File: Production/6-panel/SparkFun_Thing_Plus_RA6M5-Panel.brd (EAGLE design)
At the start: 83.3 x 181.6 mm, 1092 parts, among them J1 USB Female Type C Connector, J11 QWIIC_RA, J12 MICRO-SDFRICTION, J13 CONN_03X2, J15 THING_PLUS_LOGICAL, J16 USB Female Type C Connector, J18 QWIIC_RA, J19 MICRO-SDFRICTION, J2 THING_PLUS_LOGICAL, J20 CONN_03X2, J22 THING_PLUS_LOGICAL, J23 USB Female Type C Connector, J25 QWIIC_RA, J26 MICRO-SDFRICTION, J27 CONN_03X2, J29 THING_PLUS_LOGICAL, J3 QWIIC_RA, J30 USB Female Type C Connector, J32 QWIIC_RA, J33 MICRO-SDFRICTION, J34 CONN_03X2, J36 THING_PLUS_LOGICAL, J37 USB Female Type C Connector, J39 QWIIC_RA, J4 CONN_03X2, J40 MICRO-SDFRICTION, J41 CONN_03X2, J7 MICRO-SDFRICTION, J8 THING_PLUS_LOGICAL, J9 USB Female Type C Connector, Q1 20V/4.2A/52mΩ/1.4W, Q10 20V/4.2A/52mΩ/1.4W, Q11 20V/4.2A/52mΩ/1.4W, Q12 20V/4.2A/52mΩ/1.4W, Q2 20V/4.2A/52mΩ/1.4W, Q3 20V/4.2A/52mΩ/1.4W, Q4 20V/4.2A/52mΩ/1.4W, Q5 20V/4.2A/52mΩ/1.4W, Q6 20V/4.2A/52mΩ/1.4W, Q7 20V/4.2A/52mΩ/1.4W, Q8 20V/4.2A/52mΩ/1.4W, Q9 20V/4.2A/52mΩ/1.4W, U1 R7FA6M5, U10 MCP73831, U11 MAX17048, U12 DA14531MOD, U13 MX25L12833F 128Mb, U14 R7FA6M5, U15 RT9080-33GJ5, U16 LM66200, U17 RT9080-33GJ5, U18 MCP73831, U19 MAX17048, U2 DA14531MOD, U20 DA14531MOD, U21 MX25L12833F 128Mb, U22 R7FA6M5, U23 RT9080-33GJ5, U24 LM66200, U25 RT9080-33GJ5, U26 MCP73831, U27 MAX17048, U28 DA14531MOD, U29 MX25L12833F 128Mb, U3 MCP73831, U30 R7FA6M5, U31 RT9080-33GJ5, U32 LM66200, U33 RT9080-33GJ5, U34 MCP73831, U35 MAX17048, U36 DA14531MOD, U37 MX25L12833F 128Mb, U38 R7FA6M5, U39 RT9080-33GJ5, U4 RT9080-33GJ5, U40 LM66200, U41 RT9080-33GJ5, U42 MCP73831, U43 MAX17048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

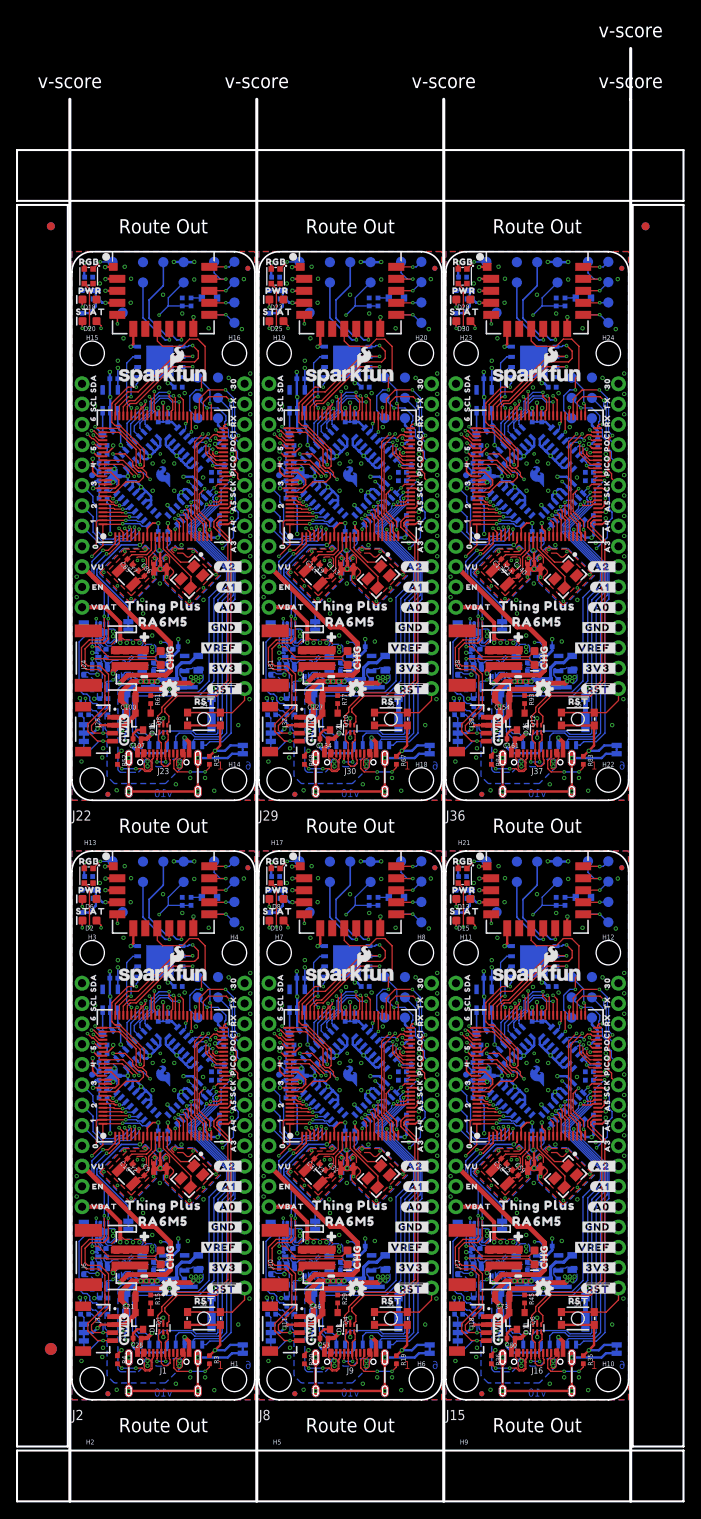
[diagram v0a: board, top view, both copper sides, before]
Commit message: Repanelize post reds review.
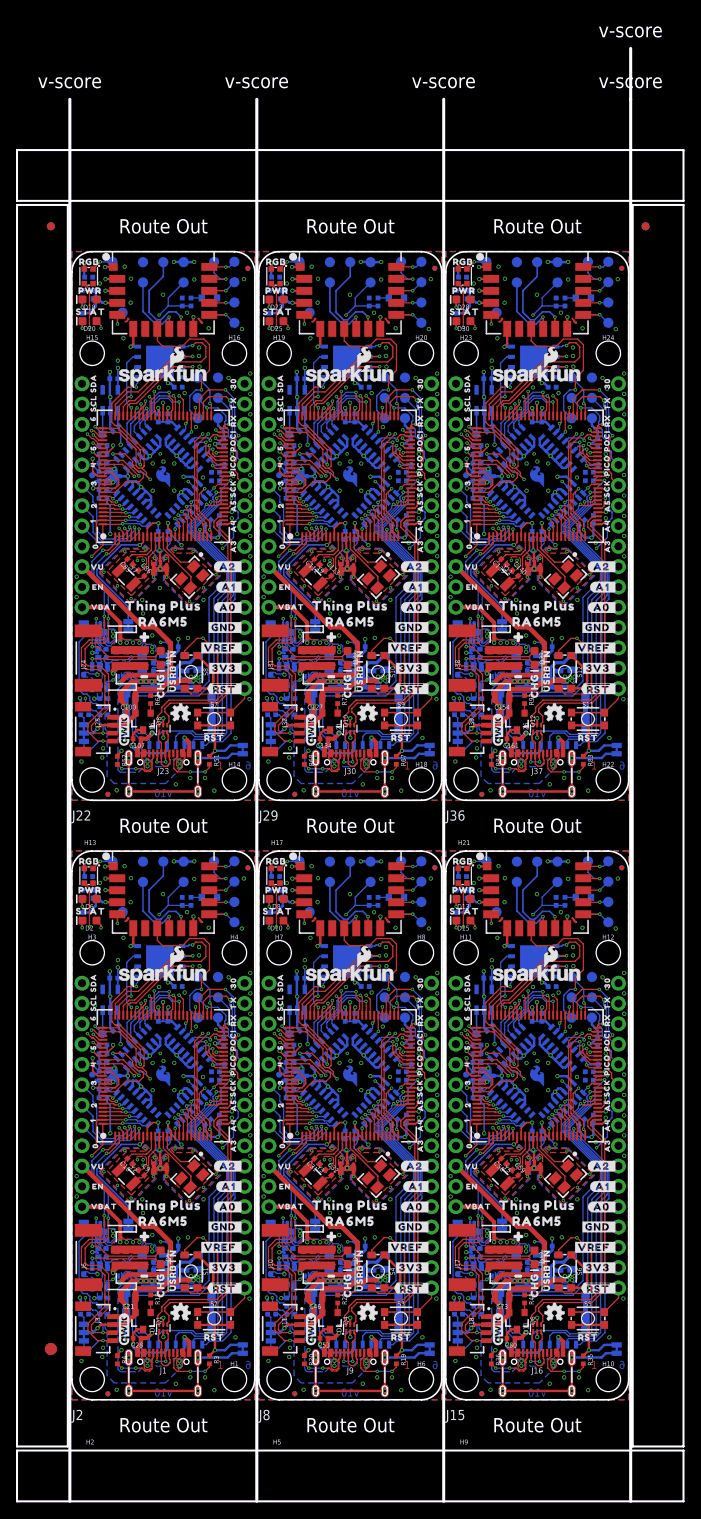
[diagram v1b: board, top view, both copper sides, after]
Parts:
- added S10, S12, S8: USER, SparkFun-Switches:TACTILE_SWITCH_SMD_4.6X2.8MM
- added S11, S7, S9: RESET, SparkFun-Switches:TACTILE_SWITCH_SMD_4.6X2.8MM
- added U$457: (no value), output:30
- added U$458: (no value), output:20
- added U$459: (no value), output:#1#0
- added U$460: (no value), output:#0#0
- added U$461: (no value), output:#USRBTN#0
- added U$462: (no value), output:#_VR#0
- S1, S4, S6: value RESET -> USER
- U$100, U$199: device output:SDA0 -> output:TX0
- U$101, U$200: device output:SCL0 -> output:SDA0
- U$102: device output:VU0 -> output:SCL0
- U$103: device output:EN0 -> output:VU0
- U$104: device output:VBAT0 -> output:EN0
- U$105: device output:#PWR#0 -> output:VBAT0
- U$106: device output:#BAT#0 -> output:#PWR#0
- U$107: device output:#SHLD#0 -> output:#BAT#0
- U$108: device output:#RST#0 -> output:#SHLD#0
- U$109: device output:#_3V3#0 -> output:#RST#0
- U$110: device output:VREF0 -> output:#_3V3#0
- U$153: device output:#I�C#0 -> output:#USRBTN#0
- U$154: device output:#CHG#0 -> output:#_VR#0
- U$155: device SparkFun-Aesthetics:SFE_LOGO_FLAME_COPPER_EXPOSED_.1 -> output:#I�C#0
- U$156: device output:#RST#0 -> output:#CHG#0
- U$157: device output:CHG0 -> SparkFun-Aesthetics:SFE_LOGO_FLAME_COPPER_EXPOSED_.1
- U$158: device output:STAT0 -> output:#RST#0
- U$159: device output:PWR0 -> output:CHG0
- U$160: device output:RGB0 -> output:STAT0
- U$161: device output:##RST#_#0 -> output:PWR0
- U$162: device output:#3V3_#0 -> output:RGB0
- U$163: device output:#VREF_#0 -> output:##RST#_#0
- U$164: device output:#GND_#0 -> output:#3V3_#0
- U$165: device output:#A0_#0 -> output:#VREF_#0
- U$166: device output:#A1_#0 -> output:#GND_#0
- U$167: device output:#A2_#0 -> output:#A0_#0
- U$168: device output:A30 -> output:#A1_#0
- U$169: device output:A40 -> output:#A2_#0
- U$170: device output:A50 -> output:A30
- U$171, U$270: device output:SCK0 -> output:A40
- U$172, U$271: device output:PICO0 -> output:A50
- U$173, U$272: device output:POCI0 -> output:SCK0
- U$174, U$273: device output:RX0 -> output:PICO0
- U$175, U$274: device output:TX0 -> output:POCI0
- U$176, U$275: device output:SDA0 -> output:RX0
- U$177, U$276: device output:SCL0 -> output:TX0
- U$178: device output:VU0 -> output:SDA0
- U$179: device output:EN0 -> output:SCL0
- U$180: device output:VBAT0 -> output:VU0
- U$181: device output:#PWR#0 -> output:EN0
- U$182: device output:#BAT#0 -> output:VBAT0
- U$183: device output:#SHLD#0 -> output:#PWR#0
- U$184: device output:#RST#0 -> output:#BAT#0
- U$185: device output:#_3V3#0 -> output:#SHLD#0
- U$186: device output:VREF0 -> output:#RST#0
- U$187: device output:#_GND#0 -> output:#_3V3#0
- U$188: device output:#_A0#0 -> output:#_GND#0
- U$189: device output:#_A1#0 -> output:#_A0#0
- U$190: device output:#_A2#0 -> output:#_A1#0
- U$191: device output:#_A3#0 -> output:#_A2#0
- U$192: device output:A40 -> output:#_A3#0
- U$193, U$94: device output:A50 -> output:A40
- U$194, U$95: device output:SCK0 -> output:A50
- U$195, U$96: device output:PICO0 -> output:SCK0
- U$196, U$97: device output:POCI0 -> output:PICO0
- U$197, U$98: device output:RX0 -> output:POCI0
- U$198, U$99: device output:TX0 -> output:RX0
- U$201: device output:#VUSB#0 -> output:SCL0
- U$202: device output:#EN_#0 -> output:#VUSB#0
- U$203: device output:#VBAT_#0 -> output:#EN_#0
- U$204: device output:THING_PLUS0 -> output:#VBAT_#0
- U$205, U$436: device output:RA6M50 -> output:THING_PLUS0
- U$206: device output:SWD_RA6M50 -> output:RA6M50
- U$207: device output:SWD_BLE0 -> output:SWD_RA6M50
- U$208: device output:RA6M50 -> output:SWD_BLE0
- U$209, U$437: device output:THING0 -> output:RA6M50
- U$210: device output:PLUS0 -> output:THING0
- U$211: device output:#0 -> output:PLUS0
- U$212: device output:_#0 -> output:#0
- U$213, U$290: device output:300 -> output:_#0
- U$215, U$291: device output:60 -> output:300
- U$216, U$223: device output:50 -> output:60
- U$217, U$224: device output:40 -> output:50
- U$218, U$225: device output:30 -> output:40
- U$219, U$226: device output:20 -> output:30
- U$220: device output:10 -> output:20
- U$221: device output:00 -> output:10
- U$222: device output:60 -> output:00
- U$227: device output:#1#0 -> output:20
- U$228: device output:#0#0 -> output:#1#0
- U$229: device output:#I�C#0 -> output:#0#0
- U$230: device output:#CHG#0 -> output:#USRBTN#0
- U$231: device SparkFun-Aesthetics:SFE_LOGO_FLAME_COPPER_EXPOSED_.1 -> output:#_VR#0
- U$232: device output:#RST#0 -> output:#I�C#0
- U$233: device output:CHG0 -> output:#CHG#0
- U$234: device output:STAT0 -> SparkFun-Aesthetics:SFE_LOGO_FLAME_COPPER_EXPOSED_.1
- U$235: device output:PWR0 -> output:#RST#0
- U$236: device output:RGB0 -> output:CHG0
- U$237: device output:##RST#_#0 -> output:STAT0
- U$238: device output:#3V3_#0 -> output:PWR0
- U$239: device output:#VREF_#0 -> output:RGB0
- U$240: device output:#GND_#0 -> output:##RST#_#0
- U$241: device output:#A0_#0 -> output:#3V3_#0
- U$242: device output:#A1_#0 -> output:#VREF_#0
- U$243: device output:#A2_#0 -> output:#GND_#0
- U$244: device output:A30 -> output:#A0_#0
- U$245: device output:A40 -> output:#A1_#0
- U$246: device output:A50 -> output:#A2_#0
- U$247: device output:SCK0 -> output:A30
- U$248, U$347: device output:PICO0 -> output:A40
- U$249, U$348: device output:POCI0 -> output:A50
- U$250, U$349: device output:RX0 -> output:SCK0
- U$251, U$350: device output:TX0 -> output:PICO0
- U$252, U$351: device output:SDA0 -> output:POCI0
- U$253, U$352: device output:SCL0 -> output:RX0
- U$254: device output:VU0 -> output:TX0
- U$255: device output:EN0 -> output:SDA0
- U$256: device output:VBAT0 -> output:SCL0
- U$257: device output:#PWR#0 -> output:VU0
- U$258: device output:#BAT#0 -> output:EN0
- U$259: device output:#SHLD#0 -> output:VBAT0
- U$260: device output:#RST#0 -> output:#PWR#0
- U$261: device output:#_3V3#0 -> output:#BAT#0
- U$262: device output:VREF0 -> output:#SHLD#0
- U$263: device output:#_GND#0 -> output:#RST#0
- U$264: device output:#_A0#0 -> output:#_3V3#0
- U$265: device output:#_A1#0 -> output:#_GND#0
- U$266: device output:#_A2#0 -> output:#_A0#0
- U$267: device output:#_A3#0 -> output:#_A1#0
- U$268: device output:A40 -> output:#_A2#0
- U$269: device output:A50 -> output:#_A3#0
- U$277: device output:#VUSB#0 -> output:SDA0
- U$278: device output:#EN_#0 -> output:SCL0
- U$279: device output:#VBAT_#0 -> output:#VUSB#0
- U$280: device output:THING_PLUS0 -> output:#EN_#0
- U$281: device output:RA6M50 -> output:#VBAT_#0
- U$282: device output:SWD_RA6M50 -> output:THING_PLUS0
- U$283: device output:SWD_BLE0 -> output:RA6M50
- U$284: device output:RA6M50 -> output:SWD_RA6M50
- U$285: device output:THING0 -> output:SWD_BLE0
- U$286: device output:PLUS0 -> output:RA6M50
- U$287: device output:#0 -> output:THING0
- U$288: device output:_#0 -> output:PLUS0
- U$289, U$366: device output:300 -> output:#0
- U$292, U$368: device output:50 -> output:300
- U$293, U$300: device output:40 -> output:60
- U$294, U$301: device output:30 -> output:50
- U$295, U$302: device output:20 -> output:40
- U$296: device output:10 -> output:30
- U$297: device output:00 -> output:20
- U$298: device output:60 -> output:10
- U$299: device output:50 -> output:00
- U$303: device output:#1#0 -> output:30
- U$304: device output:#0#0 -> output:20
- U$305: device output:#I�C#0 -> output:#1#0
- U$306: device output:#CHG#0 -> output:#0#0
- U$307: device SparkFun-Aesthetics:SFE_LOGO_FLAME_COPPER_EXPOSED_.1 -> output:#USRBTN#0
- U$308: device output:#RST#0 -> output:#_VR#0
- U$309: device output:CHG0 -> output:#I�C#0
- U$310: device output:STAT0 -> output:#CHG#0
- U$311: device output:PWR0 -> SparkFun-Aesthetics:SFE_LOGO_FLAME_COPPER_EXPOSED_.1
- U$312: device output:RGB0 -> output:#RST#0
- U$313: device output:##RST#_#0 -> output:CHG0
- U$314: device output:#3V3_#0 -> output:STAT0
- U$315: device output:#VREF_#0 -> output:PWR0
- U$316: device output:#GND_#0 -> output:RGB0
- U$317: device output:#A0_#0 -> output:##RST#_#0
- U$318: device output:#A1_#0 -> output:#3V3_#0
- U$319: device output:#A2_#0 -> output:#VREF_#0
- U$320: device output:A30 -> output:#GND_#0
- U$321: device output:A40 -> output:#A0_#0
- U$322: device output:A50 -> output:#A1_#0
- U$323: device output:SCK0 -> output:#A2_#0
- U$324: device output:PICO0 -> output:A30
- U$325, U$424: device output:POCI0 -> output:A40
- U$326, U$425: device output:RX0 -> output:A50
- U$327, U$426: device output:TX0 -> output:SCK0
- U$328, U$427: device output:SDA0 -> output:PICO0
- U$329, U$428: device output:SCL0 -> output:POCI0
- U$330: device output:VU0 -> output:RX0
- U$331: device output:EN0 -> output:TX0
- U$332: device output:VBAT0 -> output:SDA0
- U$333: device output:#PWR#0 -> output:SCL0
- U$334: device output:#BAT#0 -> output:VU0
- U$335: device output:#SHLD#0 -> output:EN0
- U$336: device output:#RST#0 -> output:VBAT0
- U$337: device output:#_3V3#0 -> output:#PWR#0
- U$338: device output:VREF0 -> output:#BAT#0
- U$339: device output:#_GND#0 -> output:#SHLD#0
- U$340: device output:#_A0#0 -> output:#RST#0
- U$341: device output:#_A1#0 -> output:#_3V3#0
- U$342: device output:#_A2#0 -> output:#_GND#0
- U$343: device output:#_A3#0 -> output:#_A0#0
- U$344: device output:A40 -> output:#_A1#0
- U$345: device output:A50 -> output:#_A2#0
- U$346: device output:SCK0 -> output:#_A3#0
- U$353: device output:#VUSB#0 -> output:TX0
- U$354: device output:#EN_#0 -> output:SDA0
- U$355: device output:#VBAT_#0 -> output:SCL0
- U$356: device output:THING_PLUS0 -> output:#VUSB#0
- U$357: device output:RA6M50 -> output:#EN_#0
- U$358: device output:SWD_RA6M50 -> output:#VBAT_#0
- U$359: device output:SWD_BLE0 -> output:THING_PLUS0
- U$361: device output:THING0 -> output:SWD_RA6M50
- U$362: device output:PLUS0 -> output:SWD_BLE0
- U$363: device output:#0 -> output:RA6M50
- U$364: device output:_#0 -> output:THING0
- U$365, U$442: device output:300 -> output:PLUS0
- U$367: device output:60 -> output:_#0
- U$369, U$445: device output:40 -> output:300
- U$370, U$377: device output:30 -> output:60
- U$371, U$378: device output:20 -> output:50
- U$372: device output:10 -> output:40
- U$373: device output:00 -> output:30
- U$374: device output:60 -> output:20
- U$375: device output:50 -> output:10
- U$376: device output:40 -> output:00
- U$379: device output:#1#0 -> output:40
- U$380: device output:#0#0 -> output:30
- U$381: device output:#I�C#0 -> output:20
- U$382: device output:#CHG#0 -> output:#1#0
- U$383: device SparkFun-Aesthetics:SFE_LOGO_FLAME_COPPER_EXPOSED_.1 -> output:#0#0
- U$384: device output:#RST#0 -> output:#USRBTN#0
- U$385: device output:CHG0 -> output:#_VR#0
- U$386: device output:STAT0 -> output:#I�C#0
- U$387: device output:PWR0 -> output:#CHG#0
- U$388: device output:RGB0 -> SparkFun-Aesthetics:SFE_LOGO_FLAME_COPPER_EXPOSED_.1
- U$389: device output:##RST#_#0 -> output:#RST#0
- U$390: device output:#3V3_#0 -> output:CHG0
- U$391: device output:#VREF_#0 -> output:STAT0
- U$392: device output:#GND_#0 -> output:PWR0
- U$393: device output:#A0_#0 -> output:RGB0
- U$394: device output:#A1_#0 -> output:##RST#_#0
- U$395: device output:#A2_#0 -> output:#3V3_#0
- U$396: device output:A30 -> output:#VREF_#0
- U$397: device output:A40 -> output:#GND_#0
- U$398: device output:A50 -> output:#A0_#0
- U$399: device output:SCK0 -> output:#A1_#0
- U$400: device output:PICO0 -> output:#A2_#0
- U$401: device output:POCI0 -> output:A30
- U$402: device output:RX0 -> output:A40
- U$403: device output:TX0 -> output:A50
- U$404: device output:SDA0 -> output:SCK0
- U$405: device output:SCL0 -> output:PICO0
- U$406: device output:VU0 -> output:POCI0
- U$407: device output:EN0 -> output:RX0
- U$408: device output:VBAT0 -> output:TX0
- U$409: device output:#PWR#0 -> output:SDA0
- U$410: device output:#BAT#0 -> output:SCL0
- U$411: device output:#SHLD#0 -> output:VU0
- U$412: device output:#RST#0 -> output:EN0
- U$413: device output:#_3V3#0 -> output:VBAT0
- U$414: device output:VREF0 -> output:#PWR#0
- U$415: device output:#_GND#0 -> output:#BAT#0
- U$416: device output:#_A0#0 -> output:#SHLD#0
- U$417: device output:#_A1#0 -> output:#RST#0
- U$418: device output:#_A2#0 -> output:#_3V3#0
- U$419: device output:#_A3#0 -> output:#_GND#0
- U$420: device output:A40 -> output:#_A0#0
- U$421: device output:A50 -> output:#_A1#0
- U$422: device output:SCK0 -> output:#_A2#0
- U$423: device output:PICO0 -> output:#_A3#0
- U$429: device output:#VUSB#0 -> output:RX0
- U$430: device output:#EN_#0 -> output:TX0
- U$431: device output:#VBAT_#0 -> output:SDA0
- U$432: device output:THING_PLUS0 -> output:SCL0
- U$433: device output:RA6M50 -> output:#VUSB#0
- U$434: device output:SWD_RA6M50 -> output:#EN_#0
- U$435: device output:SWD_BLE0 -> output:#VBAT_#0
- U$438: device output:PLUS0 -> output:SWD_RA6M50
- U$439: device output:#0 -> output:SWD_BLE0
- U$440: device output:_#0 -> output:RA6M50
- U$441: device output:300 -> output:THING0
- U$443: device output:60 -> output:#0
- U$444: device output:50 -> output:_#0
- U$446: device output:30 -> output:300
- U$447, U$454: device output:20 -> output:60
- U$448: device output:10 -> output:50
- U$449: device output:00 -> output:40
- U$450: device output:60 -> output:30
- U$451: device output:50 -> output:20
- U$452: device output:40 -> output:10
- U$453: device output:30 -> output:00
- U$455: device output:#1#0 -> output:50
- U$456: device output:#0#0 -> output:40
- U$53: device output:VREF0 -> output:#_VR#0
- U$73: device output:PWR0 -> output:#USRBTN#0
- U$74: device output:RGB0 -> output:PWR0
- U$75: device output:##RST#_#0 -> output:RGB0
- U$80: device output:#3V3_#0 -> output:##RST#_#0
- U$87: device output:#VREF_#0 -> output:#3V3_#0
- U$88: device output:#GND_#0 -> output:#VREF_#0
- U$89: device output:#A0_#0 -> output:#GND_#0
- U$90: device output:#A1_#0 -> output:#A0_#0
- U$91: device output:#A2_#0 -> output:#A1_#0
- U$92: device output:A30 -> output:#A2_#0
- U$93: device output:A40 -> output:A30
- moved U$231 111.8 mm to (68.2, 19.1)
- moved U$230 96.5 mm to (59.2, 16.1), flipped to the top
- moved S5 78.9 mm to (64.5, 10.2)
- moved S4 72.4 mm to (38.3, 16.1), turned to 270 degrees
- moved U$229 69.3 mm to (49.5, 31.8), turned to 0 degrees
- moved S6 69.1 mm to (61.6, 16.1), turned to 270 degrees
- moved U$312 61.4 mm to (41.2, 82.8)
- moved U$235 57.9 mm to (17.8, 82.8)
- moved U$75 56.8 mm to (25.5, 67.3)
- moved U$183 55.6 mm to (52.7, 63.1), turned to 0 degrees
- moved U$158 55.4 mm to (64.5, 7.90)
- moved U$162 54.4 mm to (48.9, 67.3)
- moved U$236 53.8 mm to (11.1, 89.2), turned to 90 degrees
- moved U$161 53.4 mm to (49.0, 63.7)
- moved U$386 52.7 mm to (49.9, 83.3), flipped to the bottom, turned to 90 degrees
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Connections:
- removed net N$12 (its old number): RN3.15, U1.17
- removed net N$125 (its old number): RN12.15, U22.17
- removed net N$169 (its old number): RN16.15, U30.17
- removed net N$213 (its old number): RN20.15, U38.17
- removed net N$257 (its old number): RN24.15, U46.17
- removed net N$79 (its old number): RN8.15, U14.17
- new net !USR_BTN!: RN3.15, S1.1, S1.2, U1.17
- new net !USR_BTN!1: RN8.15, S4.1, S4.2, U14.17
- new net !USR_BTN!2: RN12.15, S6.1, S6.2, U22.17
- new net !USR_BTN!3: RN16.15, S8.1, S8.2, U30.17
- new net !USR_BTN!4: RN20.15, S10.1, S10.2, U38.17
- new net !USR_BTN!5: RN24.15, S12.1, S12.2, U46.17
- net !RA6M5_RESET!1: now also S3.3, S3.4; no longer S1.3, S1.4
- net !RA6M5_RESET!2: now also S5.3, S5.4; no longer S3.3, S3.4
- net !RA6M5_RESET!3: now also S7.3, S7.4; no longer S4.3, S4.4
- net !RA6M5_RESET!4: now also S9.3, S9.4; no longer S5.3, S5.4
- net !RA6M5_RESET!5: now also S11.3, S11.4; no longer S6.3, S6.4
- net 3.3V: now also RN1.11, RN3.2
- net 3.3V1: now also RN6.11, RN8.2
- net 3.3V2: now also RN10.11, RN12.2
- net 3.3V3: now also RN14.11, RN16.2
- net 3.3V4: now also RN18.11, RN20.2
- net 3.3V5: now also RN22.11, RN24.2
- net GND: now also S1.3, S1.4; no longer RN3.2
- net GND1: now also S3.1, S3.2, S4.3, S4.4; no longer RN8.2, S1.1, S1.2
- net GND2: now also S5.1, S5.2, S6.3, S6.4; no longer RN12.2, S3.1, S3.2
- net GND3: now also S7.1, S7.2, S8.3, S8.4; no longer RN16.2, S4.1, S4.2
- net GND4: now also S10.3, S10.4, S9.1, S9.2; no longer RN20.2, S5.1, S5.2
- net GND5: now also S11.1, S11.2, S12.3, S12.4; no longer RN24.2, S6.1, S6.2
- net VIN: no longer RN1.11
- net VIN1: no longer RN6.11
- net VIN2: no longer RN10.11
- net VIN3: no longer RN14.11
- net VIN4: no longer RN18.11
- net VIN5: no longer RN22.11
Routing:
- net !USR_BTN!5: track 0.00 -> 38.6 mm, vias 0 -> 2
- net !USR_BTN!4: track 0.00 -> 38.6 mm, vias 0 -> 2
- net !USR_BTN!3: track 0.00 -> 38.6 mm, vias 0 -> 2
- net !USR_BTN!2: track 0.00 -> 38.6 mm, vias 0 -> 2
- net !USR_BTN!1: track 0.00 -> 38.6 mm, vias 0 -> 2
- net !USR_BTN!: track 0.00 -> 38.6 mm, vias 0 -> 2
- net GND4: track 152.6 -> 158.2 mm, vias 49 -> 51
- net GND2: track 152.6 -> 158.2 mm, vias 49 -> 51
- net GND: track 152.6 -> 158.2 mm, vias 49 -> 51
- net GND3: track 152.6 -> 158.2 mm, vias 49 -> 51
- net GND5: track 152.6 -> 158.2 mm, vias 49 -> 51
- net GND1: track 152.6 -> 158.2 mm, vias 49 -> 51
- net N$213 (its old number): track 3.51 -> 0.00 mm, vias 1 -> 0
- net N$169 (its old number): track 3.51 -> 0.00 mm, vias 1 -> 0
- net N$257 (its old number): track 3.51 -> 0.00 mm, vias 1 -> 0
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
